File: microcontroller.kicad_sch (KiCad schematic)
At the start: 21 parts, among them J2 675031020, J3 Conn_01x04_Pin, J4 Conn_01x04_Pin, J5 Conn_01x04_Pin, J6 Conn_01x05_Pin, SW1 SW_SPDT, SW2 SW_SPDT, U2 STM32F401RETx, Y1 16MHz

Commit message: addecd stuff
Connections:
- net 12C1_SCL renamed I2C1_SCL
- net 12C1_SDA renamed I2C1_SDA
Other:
- moved on the sheet: J6, R3, R4

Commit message: Initiliase main components
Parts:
- removed J2: 675031020, CON00317_5_MOL, symbol USBBMini:675031020
- J3: value Conn_01x04_Pin -> USART1 Header
- J4: value Conn_01x04_Pin -> I2C1 Header
- J5: value Conn_01x04_Pin -> SPI Header
- J6: value Conn_01x05_Pin -> SWD Header
- SW1: value SW_SPDT -> Boot Switch
- SW2: value SW_SPDT -> System Reset
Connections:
- no-connect marks 40 -> 39

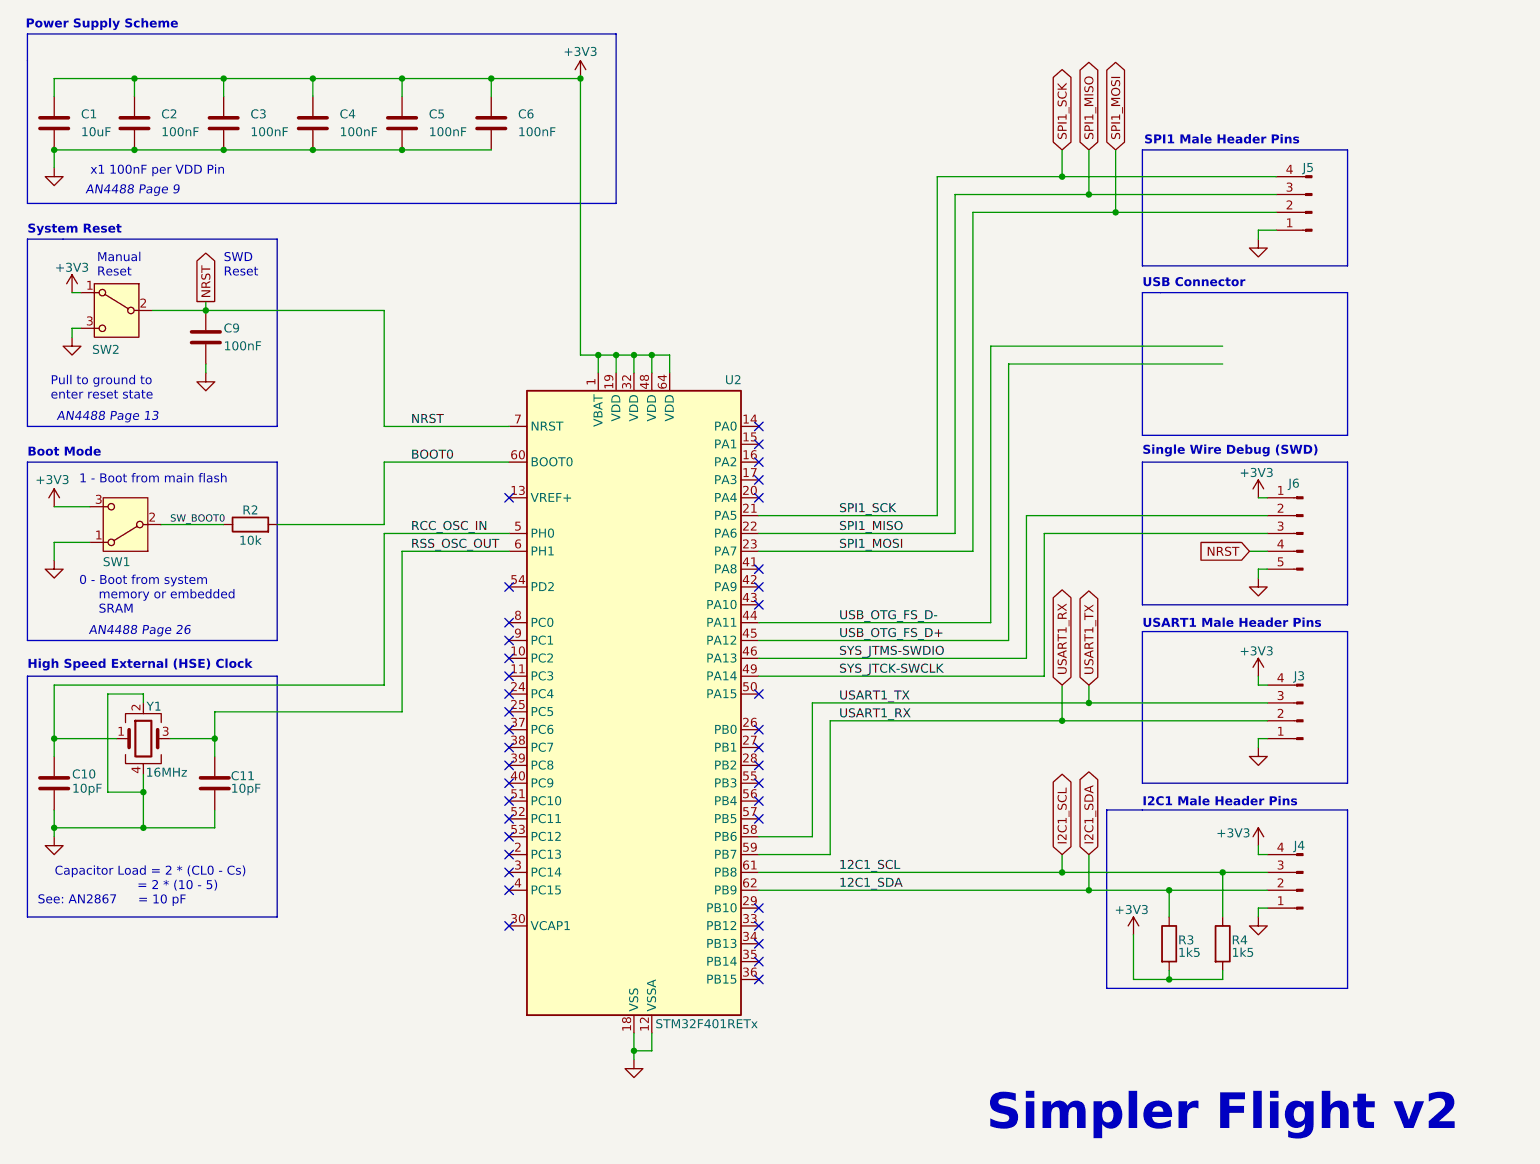
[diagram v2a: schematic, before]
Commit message: Update schematic, pending power sims, updated README
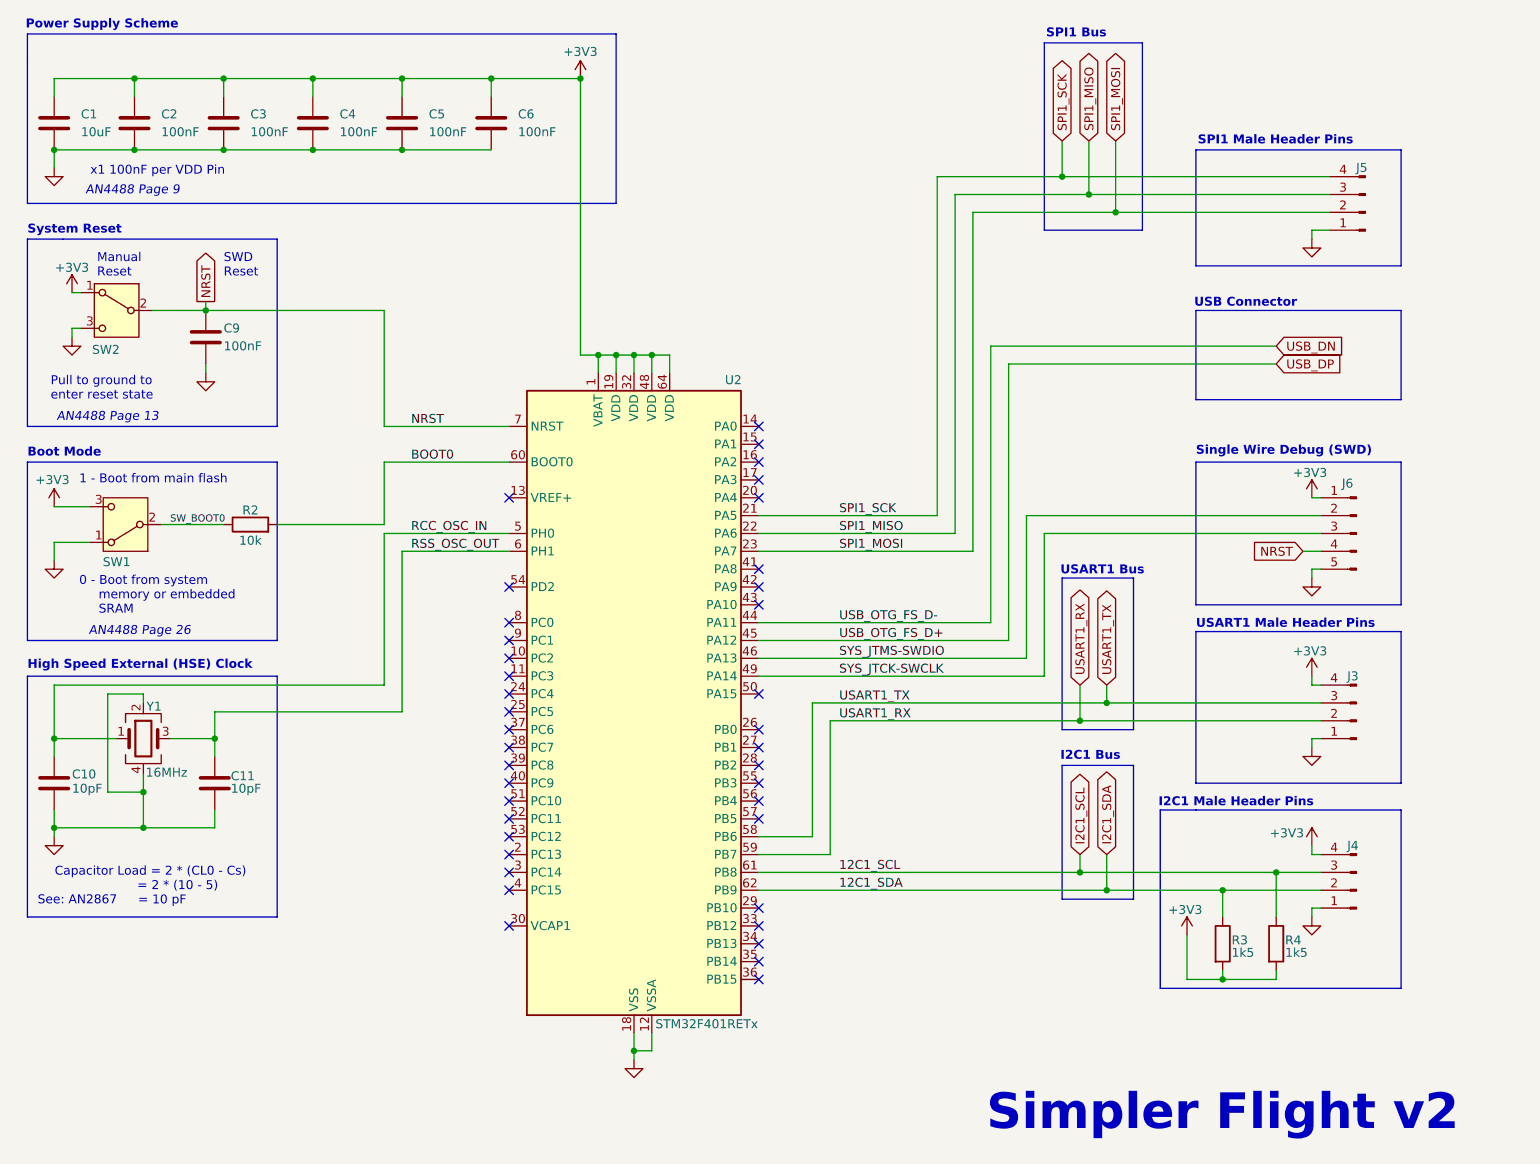
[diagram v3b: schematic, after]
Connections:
- net USB_OTG_FS_D+ renamed USB_DP
- net USB_OTG_FS_D- renamed USB_DN
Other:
- note added: "I2C1 Bus"
- note added: "SPI1 Bus"
- note added: "USART1 Bus"
- moved on the sheet: J3, J4, J5, J6, R3, R4

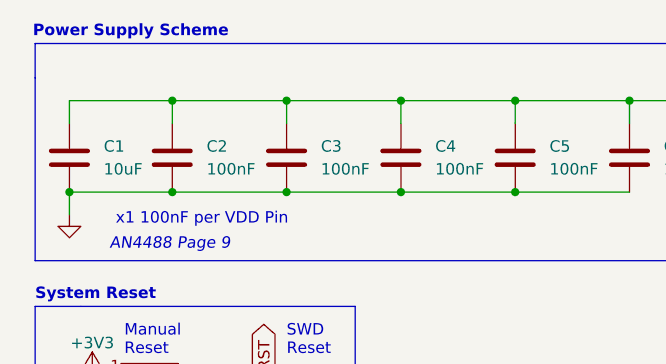
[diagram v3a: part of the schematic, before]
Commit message: Remove transistor enable for servo power. Added falstad sim files
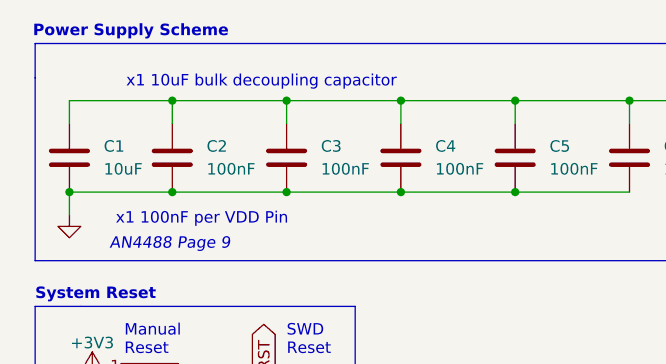
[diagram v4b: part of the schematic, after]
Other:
- note added: "x1 10uF bulk decoupling capacitor"
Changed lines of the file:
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@@
+		)
+	)
+	(text "x1 10uF bulk decoupling capacitor"
+		(exclude_from_sim no)
+		(at 67.056 24.638 0)
+		(effects
+			(font
+				(size 1.27 1.27)
+			)
 		)
 	)

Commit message: Updated schematics
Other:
- note added: "CAS Board 2025"
- note removed: "Simpler Flight v2"
